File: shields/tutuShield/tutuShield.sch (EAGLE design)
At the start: 5 parts

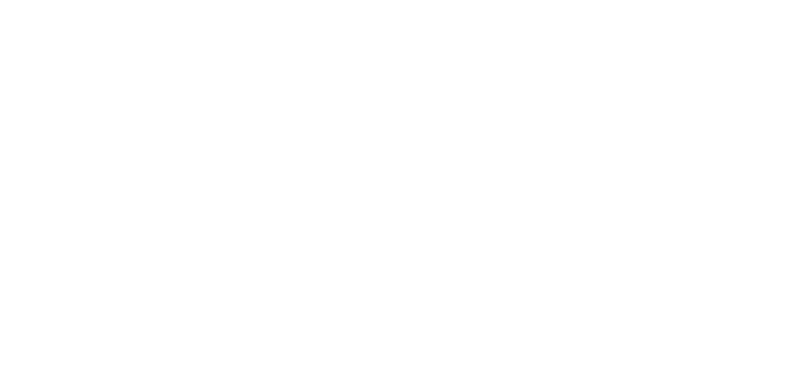
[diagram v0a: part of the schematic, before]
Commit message: added MSGEQ7 to lib
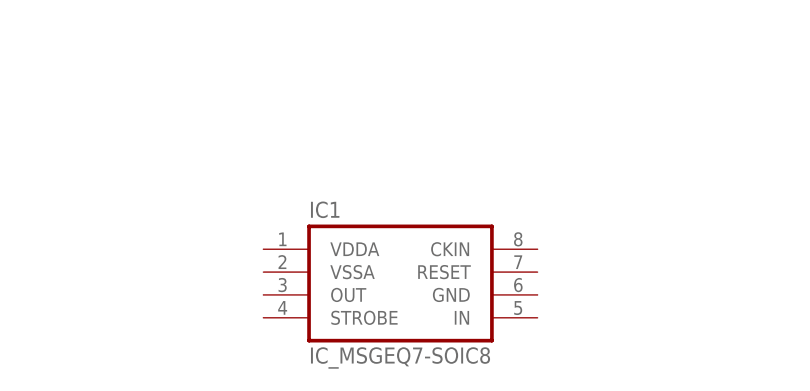
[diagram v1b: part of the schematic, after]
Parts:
- added IC1: IC_MSGEQ7-SOIC8, ATtami:IC_MSGEQ7-SOIC8
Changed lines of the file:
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@@
 <part name="J1" library="microbuilder" deviceset="HEADER-1X7" device="ROUND"/>
 <part name="GND5" library="SparkFun" deviceset="GND" device=""/>
+<part name="IC1" library="ATtami" deviceset="IC_MSGEQ7" device="-SOIC8"/>
 </parts>
 <sheets>
@@
 <instance part="J1" gate="A" x="233.68" y="121.92"/>
 <instance part="GND5" gate="1" x="218.44" y="134.62" rot="R180"/>
+<instance part="IC1" gate="IC" x="116.84" y="83.82"/>
 </instances>
 <busses>

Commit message: didn't save last time :\
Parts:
- added C1: 33pF, ATtami:CAP0805
- added C2, C4: 0.1uF, ATtami:CAP0805
- added C3: 1000pF, ATtami:CAP0805
- added JP1: (no value), ATtami:HEADER-1X2ROUND
- added R1: 200K, ATtami:RESISTOR0805-RES
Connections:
- new net CKIN: C1.1, IC1.CKIN, R1.1
- new net IN: C3.1, IC1.IN
- new net N$1: C3.2, JP1.2
- new net N$4: IC1.GND, JP1.1
- new net N$5: C2.1, IC1.VSSA
- net GND: now also C1.2, C2.2, C4.1
- net PB0: now also IC1.RESET
- net PB1: now also IC1.STROBE
- net PB2: now also IC1.OUT
- net VCC: now also C4.2, R1.2
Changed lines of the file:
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@@
 <?xml version="1.0" encoding="utf-8"?>
 <!DOCTYPE eagle SYSTEM "eagle.dtd">
-<eagle version="7.1.0">
+<eagle version="7.2.0">
 <drawing>
 <settings>
@@
 <part name="GND5" library="SparkFun" deviceset="GND" device=""/>
 <part name="IC1" library="ATtami" deviceset="IC_MSGEQ7" device="-SOIC8"/>
+<part name="C1" library="ATtami" deviceset="CAP" device="0805" value="33pF"/>
+<part name="C2" library="ATtami" deviceset="CAP" device="0805" value="0.1uF"/>
+<part name="C3" library="ATtami" deviceset="CAP" device="0805" value="1000pF"/>
+<part name="C4" library="ATtami" deviceset="CAP" device="0805" value="0.1uF"/>
+<part name="GND2" library="SparkFun" deviceset="GND" device=""/>
+<part name="JP1" library="ATtami" deviceset="HEADER-1X2" device="ROUND"/>
+<part name="R1" library="ATtami" deviceset="RESISTOR" device="0805-RES" value="200K"/>
 </parts>
 <sheets>
@@
 <instance part="GND5" gate="1" x="218.44" y="134.62" rot="R180"/>
 <instance part="IC1" gate="IC" x="116.84" y="83.82"/>
+<instance part="C1" gate="G$1" x="68.58" y="78.74"/>
+<instance part="C2" gate="G$1" x="86.36" y="71.12"/>
+<instance part="C3" gate="G$1" x="157.48" y="81.28" smashed="yes" rot="R90">
+<attribute name="NAME" x="158.496" y="85.979" size="1.778" layer="95" rot="R180"/>
+<attribute name="VALUE" x="161.036" y="78.359" size="1.778" layer="96" rot="R180"/>
+</instance>
+<instance part="C4" gate="G$1" x="83.82" y="88.9" smashed="yes" rot="R90">
+<attribute name="NAME" x="84.836" y="93.599" size="1.778" layer="95" rot="R180"/>
+<attribute name="VALUE" x="87.376" y="85.979" size="1.778" layer="96" rot="R180"/>
+</instance>
+<instance part="GND2" gate="1" x="76.2" y="66.04"/>
+<instance part="JP1" gate="G$1" x="180.34" y="81.28"/>
+<instance part="R1" gate="G$1" x="86.36" y="99.06"/>
 </instances>
 <busses>
@@
 <pinref part="GND5" gate="1" pin="GND"/>
 </segment>
+<segment>
+<pinref part="C4" gate="G$1" pin="1"/>
+<pinref part="GND2" gate="1" pin="GND"/>
+<wire x1="78.74" y1="88.9" x2="76.2" y2="88.9" width="0.1524" layer="91"/>
+<wire x1="76.2" y1="88.9" x2="76.2" y2="68.58" width="0.1524" layer="91"/>
+<label x="76.2" y="73.66" size="1.778" layer="95"/>
+<pinref part="C2" gate="G$1" pin="2"/>
+<wire x1="86.36" y1="68.58" x2="76.2" y2="68.58" width="0.1524" layer="91"/>
+<junction x="76.2" y="68.58"/>
+<pinref part="C1" gate="G$1" pin="2"/>
+<wire x1="68.58" y1="76.2" x2="68.58" y2="68.58" width="0.1524" layer="91"/>
+<wire x1="68.58" y1="68.58" x2="76.2" y2="68.58" width="0.1524" layer="91"/>
+</segment>
 </net>
 <net name="VCC" class="0">
@@
 <label x="86.868" y="145.288" size="1.778" layer="95"/>
 </segment>
+<segment>
+<pinref part="C4" gate="G$1" pin="2"/>
+<wire x1="104.14" y1="88.9" x2="91.44" y2="88.9" width="0.1524" layer="91"/>
+<label x="93.98" y="88.9" size="1.778" layer="95"/>
+<pinref part="R1" gate="G$1" pin="2"/>
+<wire x1="91.44" y1="88.9" x2="86.36" y2="88.9" width="0.1524" layer="91"/>
+<wire x1="91.44" y1="99.06" x2="91.44" y2="88.9" width="0.1524" layer="91"/>
+<junction x="91.44" y="88.9"/>
+</segment>
 </net>
 <net name="N$3" class="0">
@@
 <label x="218.44" y="127" size="1.778" layer="95"/>
 </segment>
+<segment>
+<pinref part="IC1" gate="IC" pin="RESET"/>
+<wire x1="132.08" y1="86.36" x2="142.24" y2="86.36" width="0.1524" layer="91"/>
+<label x="137.16" y="86.36" size="1.778" layer="95"/>
+</segment>
 </net>
 <net name="PB1" class="0">
@@
 <label x="218.44" y="124.46" size="1.778" layer="95"/>
 </segment>
+<segment>
+<pinref part="IC1" gate="IC" pin="STROBE"/>
+<wire x1="101.6" y1="81.28" x2="96.52" y2="81.28" width="0.1524" layer="91"/>
+<label x="96.52" y="81.28" size="1.778" layer="95"/>
+</segment>
 </net>
 <net name="PB2" class="0">
@@
 <label x="218.44" y="121.92" size="1.778" layer="95"/>
 </segment>
+<segment>
+<pinref part="IC1" gate="IC" pin="OUT"/>
+<wire x1="101.6" y1="83.82" x2="99.06" y2="83.82" width="0.1524" layer="91"/>
+<label x="96.52" y="83.82" size="1.778" layer="95"/>
+</segment>
 </net>
 <net name="PB3" class="0">
@@
 </segment>
 </net>
+<net name="IN" class="0">
+<segment>
+<pinref part="IC1" gate="IC" pin="IN"/>
+<pinref part="C3" gate="G$1" pin="1"/>
+<wire x1="132.08" y1="81.28" x2="152.4" y2="81.28" width="0.1524" layer="91"/>
+</segment>
+</net>
+<net name="N$1" class="0">
+<segment>
+<pinref part="C3" gate="G$1" pin="2"/>
+<pinref part="JP1" gate="G$1" pin="2"/>
+<wire x1="160.02" y1="81.28" x2="177.8" y2="81.28" width="0.1524" layer="91"/>
+</segment>
+</net>
+<net name="N$4" class="0">
+<segment>
+<pinref part="IC1" gate="IC" pin="GND"/>
+<pinref part="JP1" gate="G$1" pin="1"/>
+<wire x1="132.08" y1="83.82" x2="177.8" y2="83.82" width="0.1524" layer="91"/>
+</segment>
+</net>
+<net name="N$5" class="0">
+<segment>
+<pinref part="C2" gate="G$1" pin="1"/>
+<wire x1="86.36" y1="76.2" x2="86.36" y2="81.28" width="0.1524" layer="91"/>
+<wire x1="86.36" y1="81.28" x2="91.44" y2="81.28" width="0.1524" layer="91"/>
+<wire x1="91.44" y1="81.28" x2="91.44" y2="86.36" width="0.1524" layer="91"/>
+<pinref part="IC1" gate="IC" pin="VSSA"/>
+<wire x1="91.44" y1="86.36" x2="101.6" y2="86.36" width="0.1524" layer="91"/>
+</segment>
+</net>
+<net name="CKIN" class="0">
+<segment>
+<pinref part="IC1" gate="IC" pin="CKIN"/>
+<wire x1="132.08" y1="88.9" x2="134.62" y2="88.9" width="0.1524" layer="91"/>
+<wire x1="134.62" y1="88.9" x2="134.62" y2="106.68" width="0.1524" layer="91"/>
+<pinref part="C1" gate="G$1" pin="1"/>
+<wire x1="134.62" y1="106.68" x2="68.58" y2="106.68" width="0.1524" layer="91"/>
+<wire x1="68.58" y1="106.68" x2="68.58" y2="99.06" width="0.1524" layer="91"/>
+<pinref part="R1" gate="G$1" pin="1"/>
+<wire x1="68.58" y1="99.06" x2="68.58" y2="83.82" width="0.1524" layer="91"/>
+<wire x1="68.58" y1="99.06" x2="81.28" y2="99.06" width="0.1524" layer="91"/>
+<junction x="68.58" y="99.06"/>
+</segment>
+</net>

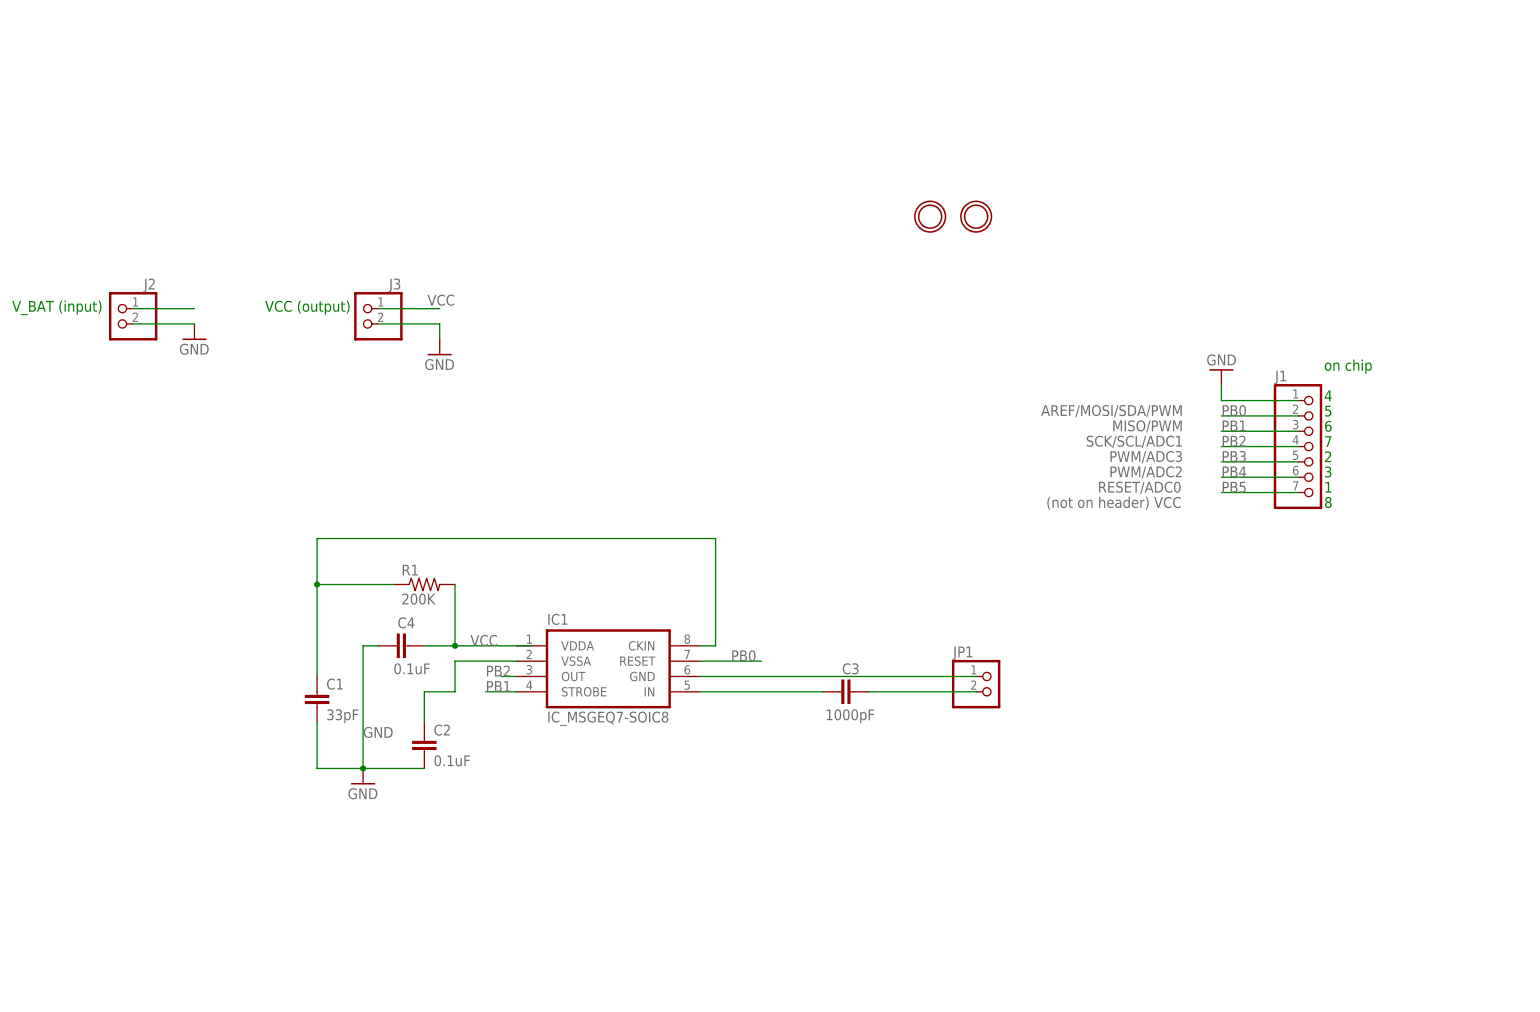
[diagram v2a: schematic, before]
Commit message: added the pb5 as digitall/reset pin thing
also text comments
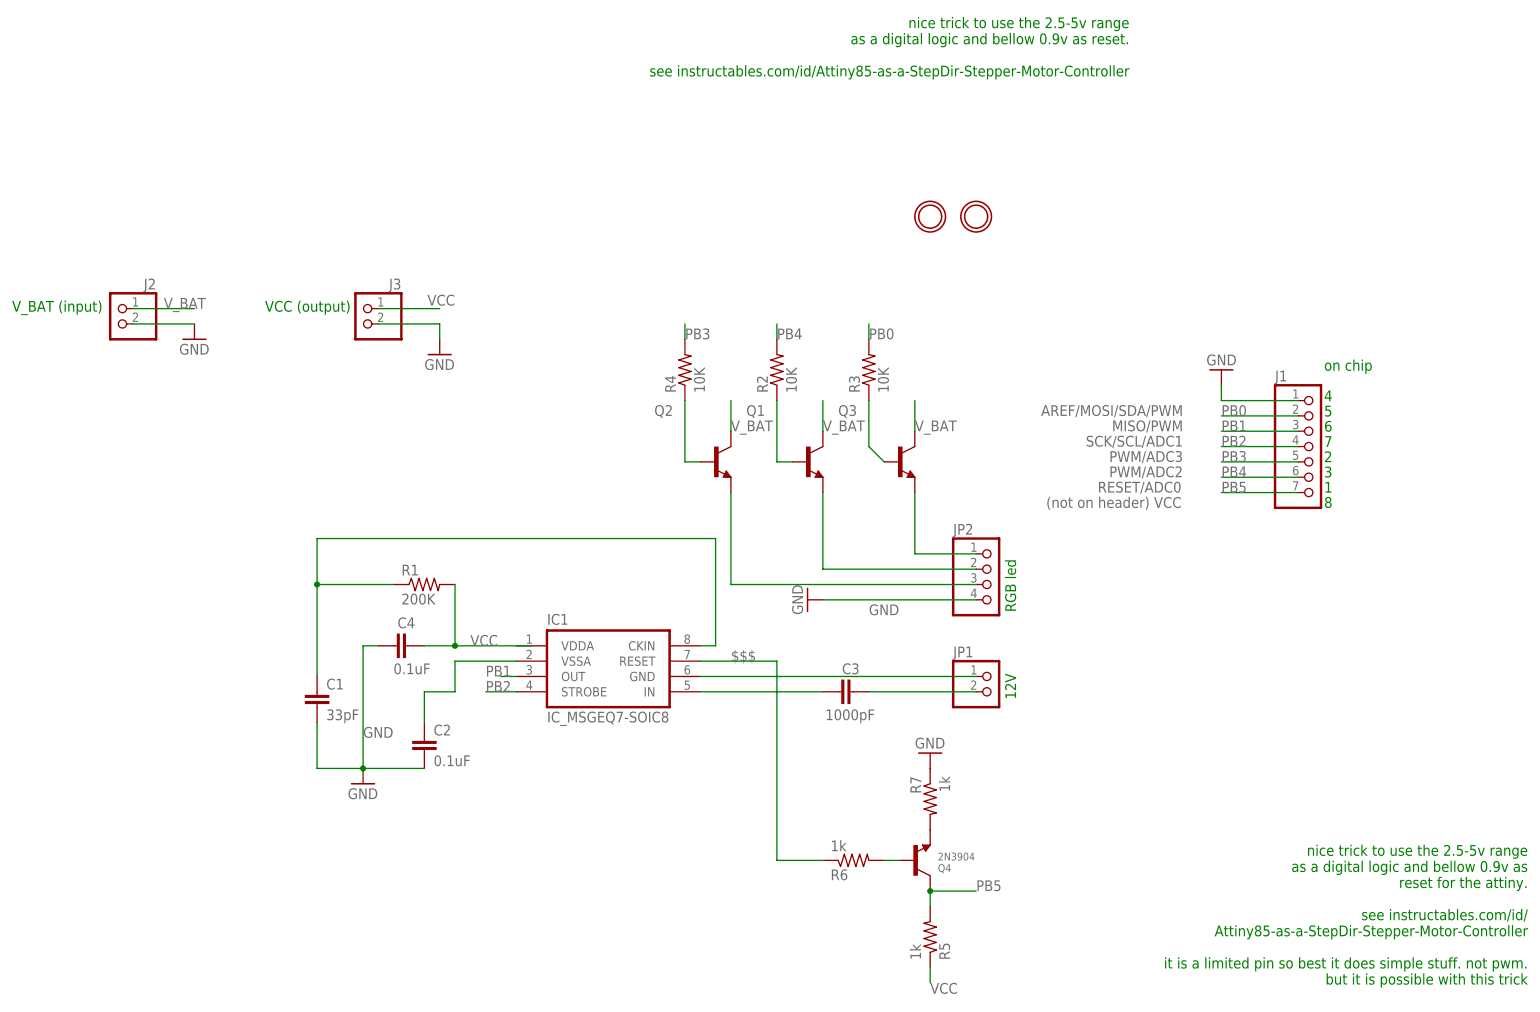
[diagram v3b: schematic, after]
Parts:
- added JP2: (no value), ATtami:HEADER-1X4ROUND
- added Q1, Q2, Q3: (no value), dp_devices:TRANSISTOR_BJT_NPN-SOT-23-BEC
- added Q4: 2N3904, microbuilder:TRANSISTOR_NPNWAVE
- added R2, R3, R4: 10K, ATtami:RESISTOR0805-RES
- added R5, R6, R7: 1k, adafruit:R-US_R0805
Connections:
- removed net N$1: C3.2, JP1.2
- new net $$$: IC1.RESET, R6.1
- new net N$10: JP2.3, Q2.E
- new net N$11: JP2.2, Q1.E
- new net N$13: JP2.1, Q3.E
- new net N$14: Q4.B, R6.2
- new net N$6: Q1.B, R2.1
- new net N$7: Q2.B, R4.1
- new net N$8: Q4.E, R7.2
- new net V_BAT: J2.1, Q1.C, Q2.C, Q3.C
- net GND: now also JP2.4, R7.1
- net N$3: now also Q3.B, R3.1; no longer J2.1
- net PB0: now also R3.2; no longer IC1.RESET
- net PB1: now also IC1.OUT; no longer IC1.STROBE
- net PB2: now also IC1.STROBE; no longer IC1.OUT
- net PB3: now also R4.2
- net PB4: now also R2.2
- net PB5: now also Q4.C, R5.2
- net VCC: now also C3.2, JP1.2, R5.1
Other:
- note added: "12V"
- note added: "RGB led"
- note added: "nice trick to use the 2.5-5v range as a digital logic and bellow 0.9v as reset for the attiny. see instructables.com/id/ Attiny85-as-a-StepDir-Stepper-Motor-Controller it is a limited pin so best it does simple stuff. not pwm. but it is possible with this trick"
- note added: "nice trick to use the 2.5-5v range as a digital logic and bellow 0.9v as reset. see instructables.com/id/Attiny85-as-a-StepDir-Stepper-Motor-Controller"

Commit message: sorry, i mixed signals
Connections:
- removed net $$$: IC1.RESET, R6.1
- net PB1: now also IC1.RESET, R6.1
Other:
- note added: "audio"
- note added: "nice trick to use the 2.5-5v range as an ADC/ logic input to the attiny and below 0.9v as reset for the attiny. see instructables.com/id/ Attiny85-as-a-StepDir-Stepper-Motor-Controller"
- note removed: "12V"
- note removed: "nice trick to use the 2.5-5v range as a digital logic and bellow 0.9v as reset for the attiny. see instructables.com/id/ Attiny85-as-a-StepDir-Stepper-Motor-Controller it is a limited pin so best it does simple stuff. not pwm. but it is possible with this trick"
- moved on the sheet: Q4, R5, R6, R7
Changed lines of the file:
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@@
 as a digital logic and bellow 0.9v as reset.
 see instructables.com/id/Attiny85-as-a-StepDir-Stepper-Motor-Controller</text>
-<text x="269.24" y="55.88" size="1.778" layer="91" rot="R180">nice trick to use the 2.5-5v range
-as a digital logic and bellow 0.9v as
-reset for the attiny.
+<text x="213.36" y="68.58" size="1.778" layer="91" rot="R180">nice trick to use the 2.5-5v range
+as an ADC/ logic input to the attiny
+and below 0.9v as reset for the attiny.
 see instructables.com/id/
 Attiny85-as-a-StepDir-Stepper-Motor-Controller
-it is a limited pin so best it does simple stuff. not pwm.
-but it is possible with this trick</text>
-<text x="184.404" y="80.01" size="1.778" layer="91" rot="R90">12V</text>
+</text>
+<text x="184.404" y="80.01" size="1.778" layer="91" rot="R90">audio</text>
 <text x="184.404" y="94.488" size="1.778" layer="91" rot="R90">RGB led </text>
 </plain>
@@
 <instance part="JP2" gate="A" x="180.34" y="104.14"/>
 <instance part="GND3" gate="1" x="149.86" y="96.52" rot="R270"/>
-<instance part="R5" gate="G$1" x="170.18" y="40.64" rot="MR90"/>
-<instance part="Q4" gate="G$1" x="170.18" y="53.34" rot="MR180"/>
-<instance part="R6" gate="G$1" x="157.48" y="53.34" rot="MR180"/>
-<instance part="R7" gate="G$1" x="170.18" y="63.5" rot="MR270"/>
-<instance part="GND4" gate="1" x="170.18" y="71.12" rot="MR180"/>
+<instance part="R5" gate="G$1" x="134.62" y="40.64" rot="MR90"/>
+<instance part="Q4" gate="G$1" x="134.62" y="53.34" rot="MR180"/>
+<instance part="R6" gate="G$1" x="121.92" y="53.34" rot="MR180"/>
+<instance part="R7" gate="G$1" x="134.62" y="63.5" rot="MR270"/>
+<instance part="GND4" gate="1" x="134.62" y="71.12" rot="MR180"/>
 </instances>
 <busses>
@@
 <segment>
 <pinref part="R5" gate="G$1" pin="1"/>
-<wire x1="170.18" y1="35.56" x2="170.18" y2="33.02" width="0.1524" layer="91"/>
-<label x="170.18" y="33.02" size="1.778" layer="95" rot="MR180"/>
+<wire x1="134.62" y1="35.56" x2="134.62" y2="33.02" width="0.1524" layer="91"/>
+<label x="134.62" y="33.02" size="1.778" layer="95" rot="MR180"/>
 </segment>
 <segment>
@@
 <segment>
 <pinref part="IC1" gate="IC" pin="OUT"/>
-<wire x1="101.6" y1="83.82" x2="99.06" y2="83.82" width="0.1524" layer="91"/>
-<label x="96.52" y="83.82" size="1.778" layer="95"/>
+<wire x1="101.6" y1="83.82" x2="93.98" y2="83.82" width="0.1524" layer="91"/>
+<wire x1="93.98" y1="83.82" x2="93.98" y2="76.2" width="0.1524" layer="91"/>
+<wire x1="93.98" y1="76.2" x2="104.14" y2="76.2" width="0.1524" layer="91"/>
+<wire x1="104.14" y1="76.2" x2="104.14" y2="53.34" width="0.1524" layer="91"/>
+<pinref part="R6" gate="G$1" pin="1"/>
+<wire x1="104.14" y1="53.34" x2="116.84" y2="53.34" width="0.1524" layer="91"/>
+</segment>
+<segment>
+<pinref part="IC1" gate="IC" pin="RESET"/>
+<wire x1="132.08" y1="86.36" x2="144.78" y2="86.36" width="0.1524" layer="91"/>
+<label x="139.7" y="86.36" size="1.778" layer="95"/>
 </segment>
 </net>
@@
 <pinref part="R5" gate="G$1" pin="2"/>
 <pinref part="Q4" gate="G$1" pin="C"/>
-<wire x1="170.18" y1="45.72" x2="170.18" y2="48.26" width="0.1524" layer="91"/>
-<wire x1="170.18" y1="48.26" x2="177.8" y2="48.26" width="0.1524" layer="91"/>
-<junction x="170.18" y="48.26"/>
-<label x="177.8" y="48.26" size="1.778" layer="95"/>
+<wire x1="134.62" y1="45.72" x2="134.62" y2="48.26" width="0.1524" layer="91"/>
+<wire x1="134.62" y1="48.26" x2="142.24" y2="48.26" width="0.1524" layer="91"/>
+<junction x="134.62" y="48.26"/>
+<label x="142.24" y="48.26" size="1.778" layer="95"/>
 </segment>
 </net>
@@
 <pinref part="Q4" gate="G$1" pin="B"/>
 <pinref part="R6" gate="G$1" pin="2"/>
-<wire x1="165.1" y1="53.34" x2="162.56" y2="53.34" width="0.1524" layer="91"/>
-</segment>
-</net>
-<net name="$$$" class="0">
-<segment>
-<pinref part="IC1" gate="IC" pin="RESET"/>
-<wire x1="132.08" y1="86.36" x2="144.78" y2="86.36" width="0.1524" layer="91"/>
-<label x="137.16" y="86.36" size="1.778" layer="95"/>
-<wire x1="144.78" y1="86.36" x2="144.78" y2="53.34" width="0.1524" layer="91"/>
-<pinref part="R6" gate="G$1" pin="1"/>
-<wire x1="144.78" y1="53.34" x2="152.4" y2="53.34" width="0.1524" layer="91"/>
-</segment>
-</net>
+<wire x1="129.54" y1="53.34" x2="127" y2="53.34" width="0.1524" layer="91"/>
+</segment>
+</net>
